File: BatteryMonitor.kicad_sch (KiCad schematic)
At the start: 26 parts, among them J5 Fuel Gauge Programming Header, U5 MAX17205

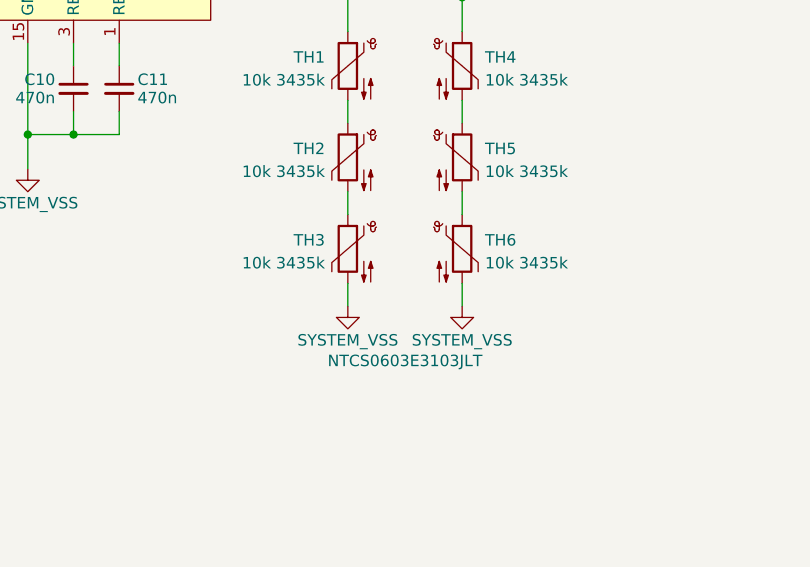
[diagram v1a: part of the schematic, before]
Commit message: Replaced old Interfaces with MCU
Added STM32U375CET6 mcu to board controlling the heaters and charging based on fuel gauge output.

Uses CAN for communication with mainboard.
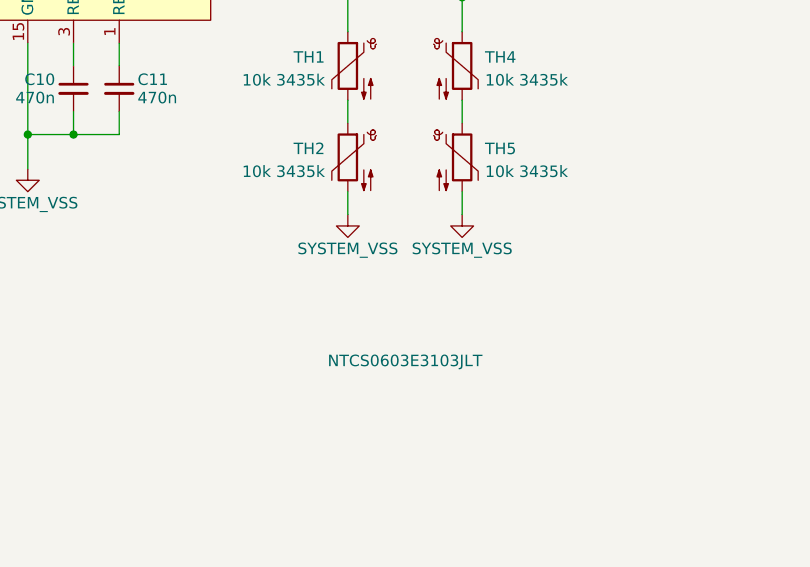
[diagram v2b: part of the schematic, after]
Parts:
- removed TH3, TH6: 10k 3435k, Capacitor_SMD:C_0603_1608Metric, symbol Device:Thermistor_NTC
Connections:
- net SYSTEM_VSS: now also TH2.2, TH5.2
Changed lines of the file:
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@@
-	(wire
-		(pts
-			(xy 132.08 143.51) (xy 132.08 146.05)
-		)
-		(stroke
-			(width 0)
-			(type default)
-		)
-	)
 	(wire
 		(pts
@@
 		(pts
 			(xy 123.19 99.06) (xy 123.19 96.52)
-		)
-		(stroke
-			(width 0)
-			(type default)
-		)
-	)
-	(wire
-		(pts
-			(xy 144.78 143.51) (xy 144.78 146.05)
 		)
 		(stroke
@@
 	)
 	(symbol
-		(lib_id "Device:Thermistor_NTC")
-		(at 144.78 139.7 0)
-		(unit 1)
-		(exclude_from_sim no)
-		(in_bom yes)
-		(on_board yes)
-		(dnp no)
-		(fields_autoplaced yes)
-		(property "Reference" "TH6"
-			(at 147.32 138.7474 0)
-			(effects
-				(font
-					(size 1.27 1.27)
-				)
-				(justify left)
-			)
-		)
-		(property "Value" "10k 3435k"
-			(at 147.32 141.2874 0)
-			(effects
-				(font
-					(size 1.27 1.27)
-				)
-				(justify left)
-			)
-		)
-		(property "Footprint" "Capacitor_SMD:C_0603_1608Metric"
-			(at 144.78 138.43 0)
-			(effects
-				(font
-					(size 1.27 1.27)
-				)
-				(hide yes)
-			)
-		)
-		(property "Datasheet" "~"
-			(at 144.78 138.43 0)
-			(effects
-				(font
-					(size 1.27 1.27)
-				)
-				(hide yes)
-			)
-		)
-		(property "Description" "Temperature dependent resistor, negative temperature coefficient"
-			(at 144.78 139.7 0)
-			(effects
-				(font
-					(size 1.27 1.27)
-				)
-				(hide yes)
-			)
-		)
-		(pin "2"
-		)
-		(pin "1"
-		)
-		(instances
-			(project "BatteryBoard"
-				(path "/b6fd875d-6e05-4440-9a05-0f0aa046a0ef/ad142cc2-d77f-4a6c-99c2-d9e17f4c27ae"
-					(reference "TH6")
-					(unit 1)
-				)
-			)
-		)
-	)
-	(symbol
 		(lib_id "power:GND")
 		(at 67.31 109.22 0)
@@
 	(symbol
 		(lib_id "power:GND")
-		(at 144.78 146.05 0)
+		(at 144.78 135.89 0)
 		(unit 1)
 		(exclude_from_sim no)
@@
 		(dnp no)
 		(property "Reference" "#PWR052"
-			(at 144.78 152.4 0)
+			(at 144.78 142.24 0)
 			(effects
 				(font
@@
 		)
 		(property "Value" "SYSTEM_VSS"
-			(at 144.78 149.86 0)
+			(at 144.78 139.7 0)
 			(effects
 				(font
@@
 		)
 		(property "Footprint" ""
-			(at 144.78 146.05 0)
+			(at 144.78 135.89 0)
 			(effects
 				(font
@@
 		)
 		(property "Datasheet" ""
-			(at 144.78 146.05 0)
+			(at 144.78 135.89 0)
 			(effects
 				(font
@@
 		)
 		(property "Description" "Power symbol creates a global label with name \"GND\" , ground"
-			(at 144.78 146.05 0)
+			(at 144.78 135.89 0)
 			(effects
 				(font
@@
 	)
 	(symbol
-		(lib_id "Device:Thermistor_NTC")
-		(at 132.08 139.7 0)
-		(mirror y)
-		(unit 1)
-		(exclude_from_sim no)
-		(in_bom yes)
-		(on_board yes)
-		(dnp no)
-		(property "Reference" "TH3"
-			(at 129.54 138.7474 0)
-			(effects
-				(font
-					(size 1.27 1.27)
-				)
-				(justify left)
-			)
-		)
-		(property "Value" "10k 3435k"
-			(at 129.54 141.2874 0)
-			(effects
-				(font
-					(size 1.27 1.27)
-				)
-				(justify left)
-			)
-		)
-		(property "Footprint" "Capacitor_SMD:C_0603_1608Metric"
-			(at 132.08 138.43 0)
-			(effects
-				(font
-					(size 1.27 1.27)
-				)
-				(hide yes)
-			)
-		)
-		(property "Datasheet" "~"
-			(at 132.08 138.43 0)
-			(effects
-				(font
-					(size 1.27 1.27)
-				)
-				(hide yes)
-			)
-		)
-		(property "Description" "Temperature dependent resistor, negative temperature coefficient"
-			(at 132.08 139.7 0)
-			(effects
-				(font
-					(size 1.27 1.27)
-				)
-				(hide yes)
-			)
-		)
-		(pin "2"
-		)
-		(pin "1"
-		)
-		(instances
-			(project "BatteryBoard"
-				(path "/b6fd875d-6e05-4440-9a05-0f0aa046a0ef/ad142cc2-d77f-4a6c-99c2-d9e17f4c27ae"
-					(reference "TH3")
-					(unit 1)
-				)
-			)
-		)
-	)
-	(symbol
 		(lib_id "Device:R_Small")
 		(at 46.99 88.9 90)
@@
 	(symbol
 		(lib_id "power:GND")
-		(at 132.08 146.05 0)
+		(at 132.08 135.89 0)
 		(unit 1)
 		(exclude_from_sim no)
@@
 		(dnp no)
 		(property "Reference" "#PWR051"
-			(at 132.08 152.4 0)
+			(at 132.08 142.24 0)
 			(effects
 				(font
@@
 		)
 		(property "Value" "SYSTEM_VSS"
-			(at 132.08 149.86 0)
+			(at 132.08 139.7 0)
 			(effects
 				(font
@@
 		)
 		(property "Footprint" ""
-			(at 132.08 146.05 0)
+			(at 132.08 135.89 0)
 			(effects
 				(font
@@
 		)
 		(property "Datasheet" ""
-			(at 132.08 146.05 0)
+			(at 132.08 135.89 0)
 			(effects
 				(font
@@
 		)
 		(property "Description" "Power symbol creates a global label with name \"GND\" , ground"
-			(at 132.08 146.05 0)
-			(effects
-				(font
+			(at 132.08 135.89 0)
+			(effects
+				(font

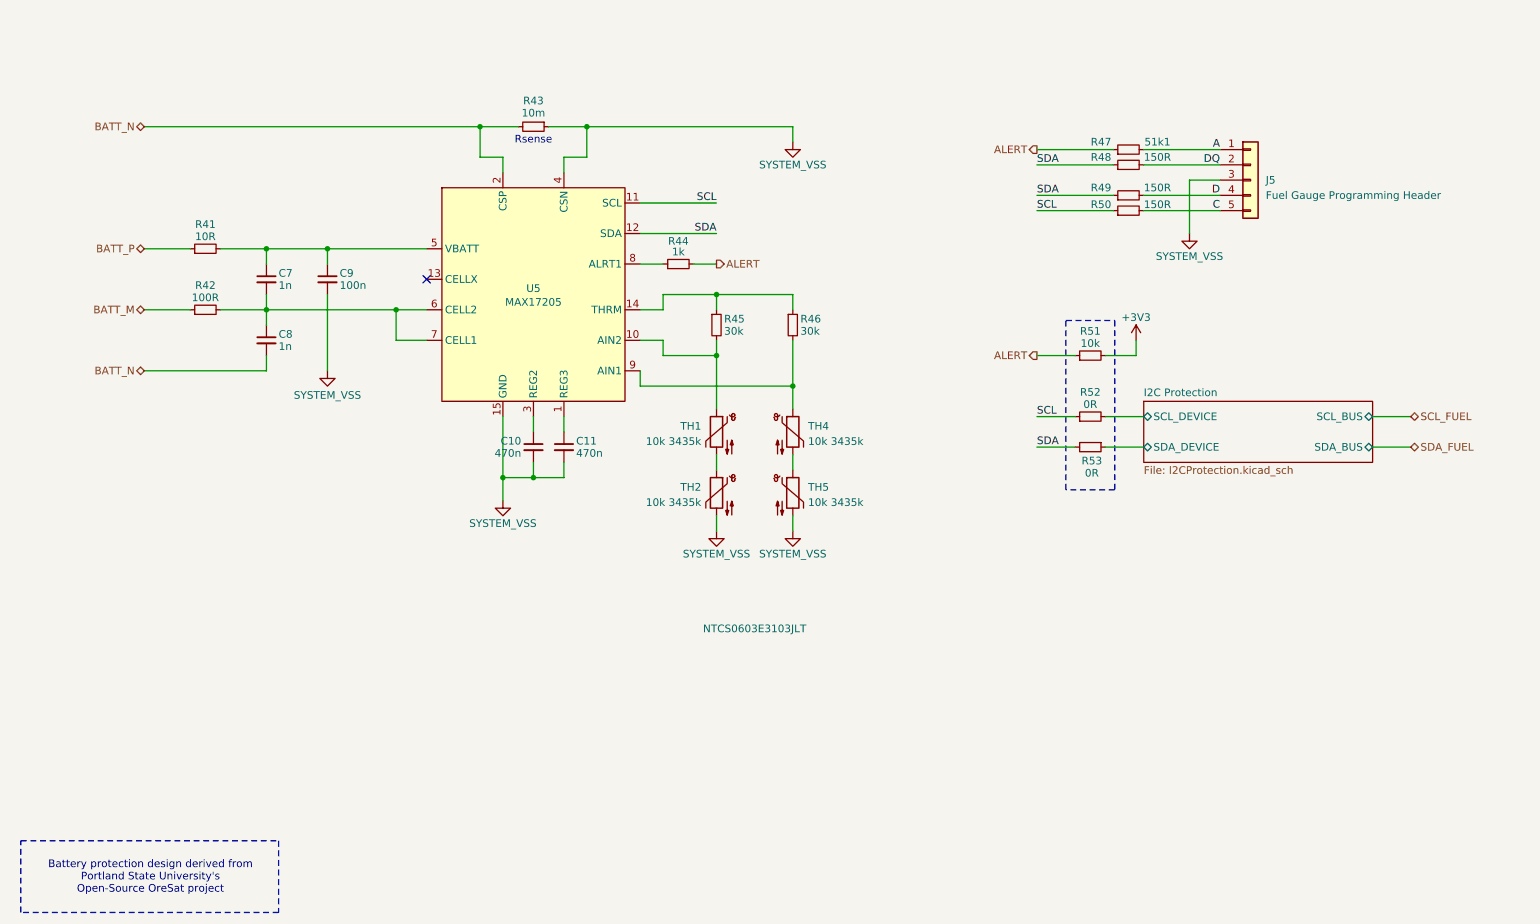
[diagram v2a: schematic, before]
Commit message: Added Schmitt Trigger mode for heaters
In the event that the mcu goes down, the thermistors will now be ale to control the heaters independently.
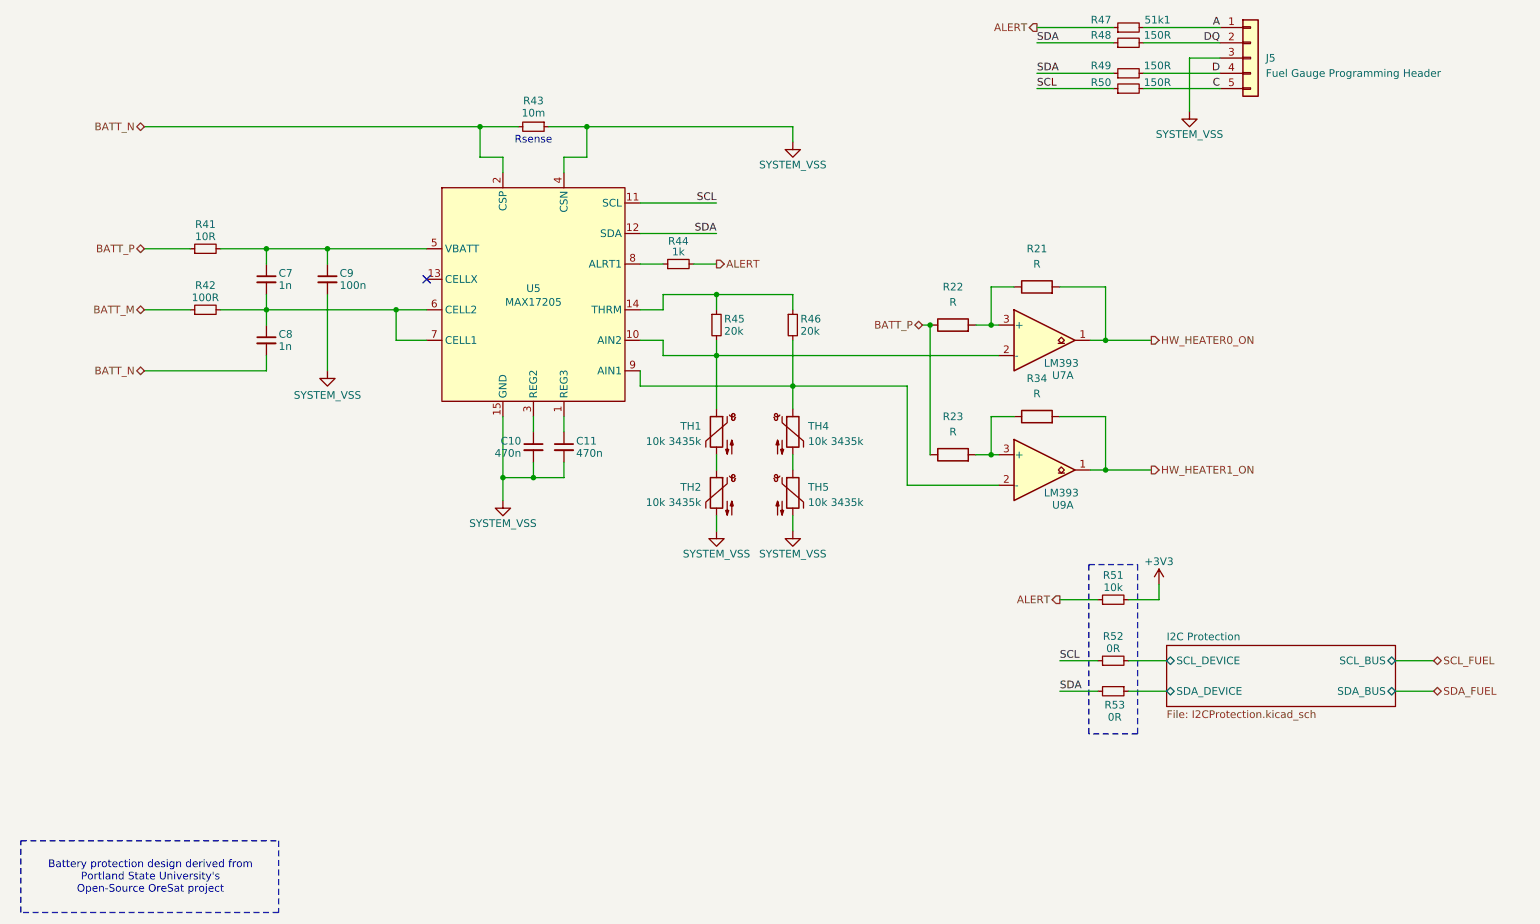
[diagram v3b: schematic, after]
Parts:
- added R21, R22, R23, R34: R, symbol Device:R
- added U7, U9: LM393, symbol Comparator:LM393
- R45, R46: value 30k -> 20k
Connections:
- net BATT_P: now also R22.1, R23.1
- net at R46.2, TH4.1, U5.9 (AIN1): now also U9.2 (-)
- net at R45.2, TH1.1, U5.10 (AIN2): now also U7.2 (-)
- new net: R23.2, R34.1, U9.3 (+)
- new net: R21.1, R22.2, U7.3 (+)
- new net HW_HEATER0_ON: R21.2, U7.1
- new net HW_HEATER1_ON: R34.2, U9.1
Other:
- moved on the sheet: J5, R47, R48, R49, R50, R51, R52, R53

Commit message: Layout in progress
In the middle of completing layout
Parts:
- R72: renamed from R22; footprint (none) -> Resistor_SMD:R_0603_1608Metric
- R73: renamed from R21; footprint (none) -> Resistor_SMD:R_0603_1608Metric
- R74: renamed from R23; footprint (none) -> Resistor_SMD:R_0603_1608Metric
- R75: renamed from R34; footprint (none) -> Resistor_SMD:R_0603_1608Metric
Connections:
- net HW_HEATER0_ON: now also R75.2, U9.1; no longer R73.2, U7.1
- net HW_HEATER1_ON: now also R73.2, U7.1; no longer R75.2, U9.1
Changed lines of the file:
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@@
+	)
+	(junction
+		(at 196.85 104.14)
+		(diameter 0)
+		(color 0 0 0 0)
 	)
 	(junction
@@
 	)
 	(junction
-		(at 196.85 125.73)
-		(diameter 0)
-		(color 0 0 0 0)
-	)
-	(junction
 		(at 101.6 127)
 		(diameter 0)
@@
 	)
 	(junction
-		(at 57.15 99.06)
+		(at 196.85 125.73)
 		(diameter 0)
 		(color 0 0 0 0)
 	)
 	(junction
-		(at 196.85 104.14)
+		(at 57.15 99.06)
 		(diameter 0)
 		(color 0 0 0 0)
@@
 	(wire
 		(pts
+			(xy 196.85 104.14) (xy 204.47 104.14)
+		)
+		(stroke
+			(width 0)
+			(type default)
+		)
+	)
+	(wire
+		(pts
 			(xy 36.83 99.06) (xy 44.45 99.06)
 		)
@@
 	(wire
 		(pts
+			(xy 196.85 125.73) (xy 204.47 125.73)
+		)
+		(stroke
+			(width 0)
+			(type default)
+		)
+	)
+	(wire
+		(pts
 			(xy 198.12 62.23) (xy 185.42 62.23)
 		)
@@
 	(wire
 		(pts
-			(xy 196.85 125.73) (xy 204.47 125.73)
-		)
-		(stroke
-			(width 0)
-			(type default)
-		)
-	)
-	(wire
-		(pts
 			(xy 67.31 88.9) (xy 67.31 91.44)
 		)
@@
 		(pts
 			(xy 200.66 162.56) (xy 207.01 162.56)
-		)
-		(stroke
-			(width 0)
-			(type default)
-		)
-	)
-	(wire
-		(pts
-			(xy 196.85 104.14) (xy 204.47 104.14)
 		)
 		(stroke
@@
 	(hierarchical_label "HW_HEATER0_ON"
 		(shape output)
-		(at 204.47 104.14 0)
+		(at 204.47 125.73 0)
 		(effects
 			(font
@@
 	(hierarchical_label "HW_HEATER1_ON"
 		(shape output)
-		(at 204.47 125.73 0)
+		(at 204.47 104.14 0)
 		(effects
 			(font
@@
 		(dnp no)
 		(fields_autoplaced yes)
-		(property "Reference" "R34"
+		(property "Reference" "R75"
 			(at 185.42 110.49 90)
 			(effects
@@
 			)
 		)
-		(property "Footprint" ""
+		(property "Footprint" "Resistor_SMD:R_0603_1608Metric"
 			(at 185.42 118.618 90)
 			(effects
@@
 			(project "Avionics-Argus3-BatteryBoard"
 				(path "/b6fd875d-6e05-4440-9a05-0f0aa046a0ef/ad142cc2-d77f-4a6c-99c2-d9e17f4c27ae"
-					(reference "R34")
+					(reference "R75")
 					(unit 1)
 				)
@@
 		(dnp no)
 		(fields_autoplaced yes)
-		(property "Reference" "R22"
+		(property "Reference" "R72"
 			(at 171.45 95.25 90)
 			(effects
@@
 			)
 		)
-		(property "Footprint" ""
+		(property "Footprint" "Resistor_SMD:R_0603_1608Metric"
 			(at 171.45 103.378 90)
 			(effects
@@
 			(project ""
 				(path "/b6fd875d-6e05-4440-9a05-0f0aa046a0ef/ad142cc2-d77f-4a6c-99c2-d9e17f4c27ae"
-					(reference "R22")
+					(reference "R72")
 					(unit 1)
 				)
@@
 		(dnp no)
 		(fields_autoplaced yes)
-		(property "Reference" "R21"
+		(property "Reference" "R73"
 			(at 185.42 88.9 90)
 			(effects
@@
 			)
 		)
-		(property "Footprint" ""
+		(property "Footprint" "Resistor_SMD:R_0603_1608Metric"
 			(at 185.42 97.028 90)
 			(effects
@@
 			(project ""
 				(path "/b6fd875d-6e05-4440-9a05-0f0aa046a0ef/ad142cc2-d77f-4a6c-99c2-d9e17f4c27ae"
-					(reference "R21")
+					(reference "R73")
 					(unit 1)
 				)
@@
 		(dnp no)
 		(fields_autoplaced yes)
-		(property "Reference" "R23"
+		(property "Reference" "R74"
 			(at 171.45 116.84 90)
 			(effects
@@
 			)
 		)
-		(property "Footprint" ""
+		(property "Footprint" "Resistor_SMD:R_0603_1608Metric"
 			(at 171.45 124.968 90)
 			(effects
@@
 			(project "Avionics-Argus3-BatteryBoard"
 				(path "/b6fd875d-6e05-4440-9a05-0f0aa046a0ef/ad142cc2-d77f-4a6c-99c2-d9e17f4c27ae"
-					(reference "R23")
+					(reference "R74")
 					(unit 1)
 				)

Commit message: finished layout
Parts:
- removed U7, U9: LM393, symbol Comparator:LM393
- added IC2: LM393WDT, SOIC127P600X175-8N, symbol LM393WDT:LM393WDT
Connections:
- net BATT_P: now also IC2.8 (VCC+)
- net HW_HEATER0_ON: now also IC2.1 (OUT1)
- net HW_HEATER1_ON: now also IC2.7 (OUT2)
- net at R74.2, R75.1: now also IC2.3 (IN1+)
- net at R46.2, TH4.1, U5.9 (AIN1): now also IC2.2 (IN1-)
- net at R72.2, R73.1: now also IC2.5 (IN2+)
- net at R45.2, TH1.1, U5.10 (AIN2): now also IC2.6 (IN2-)
- net +3V3 renamed +3.3V
- new net GND: IC2.4 (VCC-)
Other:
- moved on the sheet: R72, R73
